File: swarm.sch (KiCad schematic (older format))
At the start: 28 parts, among them P1 USB_OTG, P2 CONN_01X05, P3 CONN_02X20, SW1 SW_PUSH, U1 LM3671MF-3.3, U2 STM32F103RETx, U3 APA102, Y1 Crystal

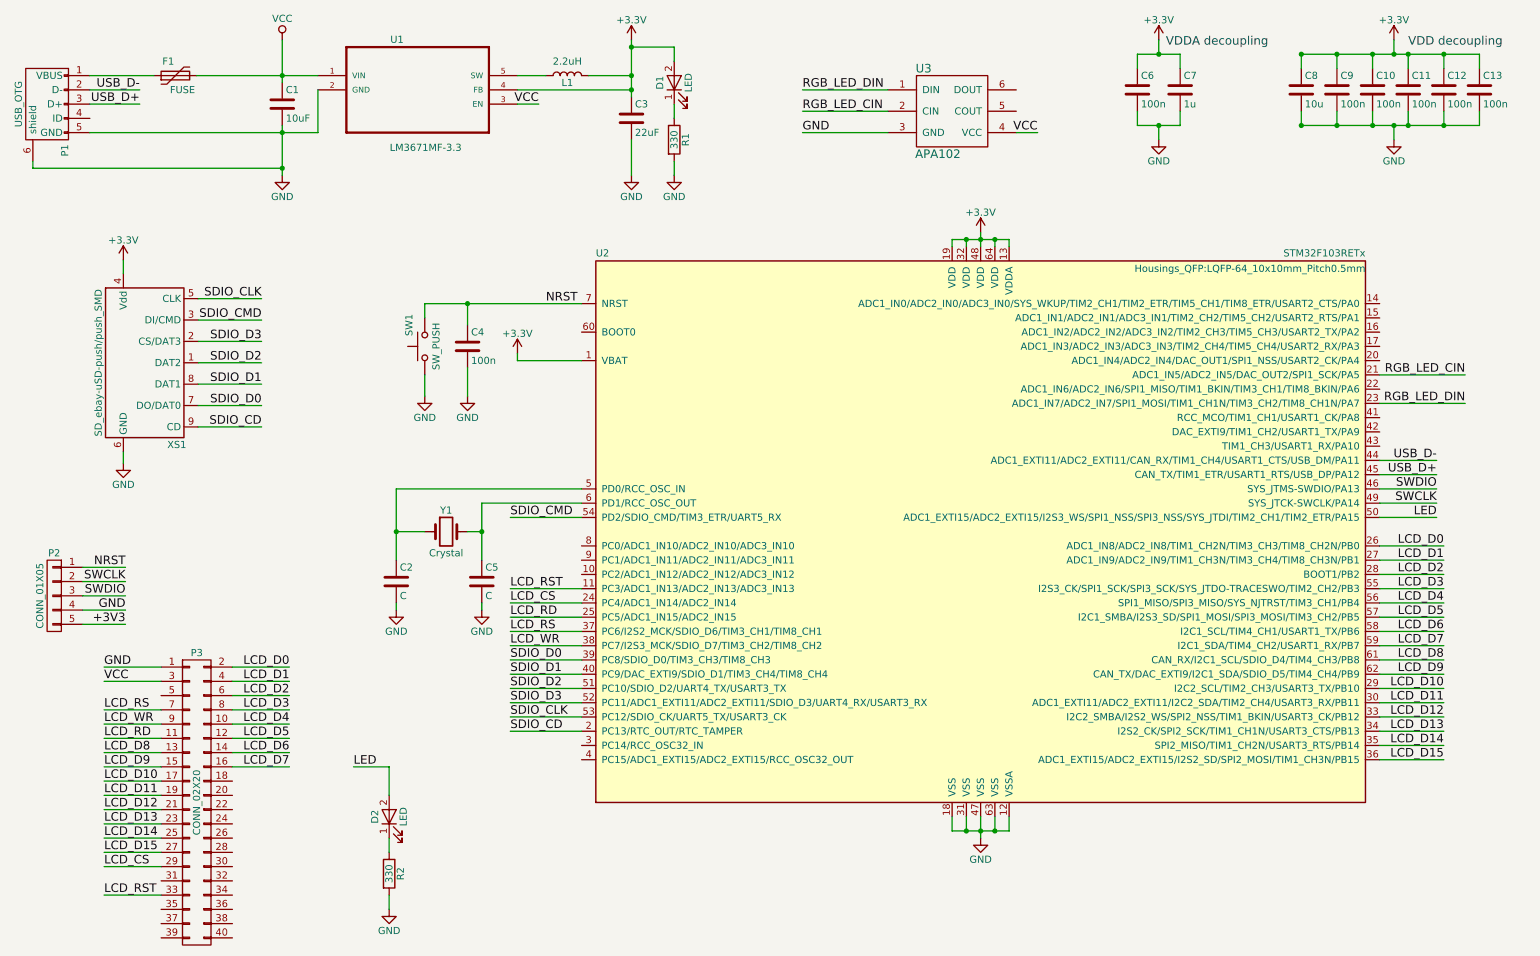
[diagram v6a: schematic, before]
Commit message: Connects 'BOOT0' pin (60) to ground Forgot to connect this pin in Rev 1.0, this pin need to be '0' to select Boot Mode "Main Flash memory" In layout, connected PIN 60 (BOOT0) to GND using 'via'
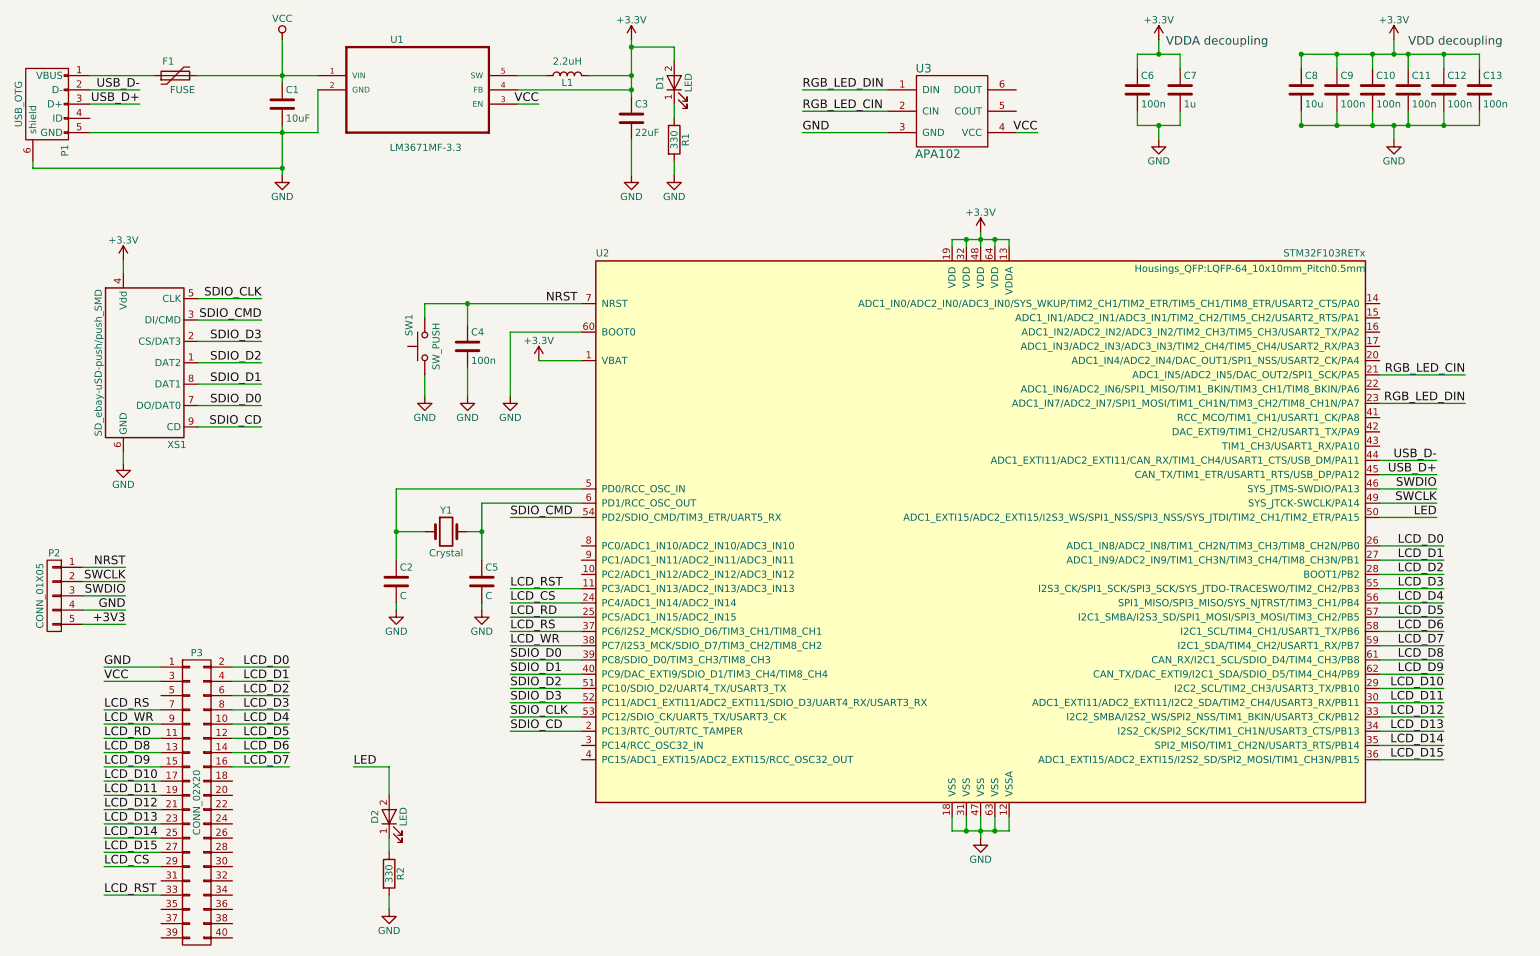
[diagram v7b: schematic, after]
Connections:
- net GND: now also U2.60 (BOOT0)
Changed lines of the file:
@@
 L +3.3V #PWR03
 U 1 1 581369FC
-P 4200 2950
-F 0 "#PWR03" H 4200 2800 50  0001 C CNN
-F 1 "+3.3V" H 4200 3090 50  0000 C CNN
-F 2 "" H 4200 2950 50  0000 C CNN
-F 3 "" H 4200 2950 50  0000 C CNN
-	1    4200 2950
+P 4350 3000
+F 0 "#PWR03" H 4350 2850 50  0001 C CNN
+F 1 "+3.3V" H 4350 3140 50  0000 C CNN
+F 2 "" H 4350 3000 50  0000 C CNN
+F 3 "" H 4350 3000 50  0000 C CNN
+	1    4350 3000
 	1    0    0    -1
 $EndComp
@@
 Connection ~ 7450 6300
 Wire Wire Line
-	7450 6200 7450 6350
+	7450 6200 7450 6300
+Wire Wire Line
+	7450 6300 7450 6350
 Connection ~ 7450 2150
 Wire Wire Line
@@
 Connection ~ 7550 2150
 Wire Wire Line
-	7450 2100 7450 2200
+	7450 2100 7450 2150
+Wire Wire Line
+	7450 2150 7450 2200
 Wire Wire Line
 	7350 2200 7350 2150
@@
 	7250 2150 7250 2200
 Wire Wire Line
-	7250 6300 7650 6300
+	7250 6300 7350 6300
+Wire Wire Line
+	7350 6300 7450 6300
+Wire Wire Line
+	7450 6300 7550 6300
+Wire Wire Line
+	7550 6300 7650 6300
 Wire Wire Line
 	7650 6300 7650 6200
@@
 Connection ~ 7550 6300
 Wire Wire Line
-	4650 3000 4200 3000
-Wire Wire Line
-	4200 3000 4200 2950
+	4650 3000 4350 3000
 Wire Wire Line
 	10700 850  10700 950
@@
 Connection ~ 10350 850
 Wire Wire Line
-	9700 1350 10950 1350
+	9700 1350 9950 1350
+Wire Wire Line
+	9950 1350 10200 1350
+Wire Wire Line
+	10200 1350 10350 1350
+Wire Wire Line
+	10350 1350 10450 1350
+Wire Wire Line
+	10450 1350 10700 1350
+Wire Wire Line
+	10700 1350 10950 1350
 Wire Wire Line
 	10700 1350 10700 1250
@@
 	3850 3050 3850 3250
 Wire Wire Line
-	3550 2600 4650 2600
+	3550 2600 3850 2600
+Wire Wire Line
+	3850 2600 4650 2600
 Wire Wire Line
 	3850 2600 3850 2750
@@
 	4650 3900 3350 3900
 Wire Wire Line
-	3350 3900 3350 4400
+	3350 3900 3350 4200
+Wire Wire Line
+	3350 4200 3350 4400
 Wire Wire Line
 	3350 4200 3550 4200
@@
 	3850 4200 3950 4200
 Wire Wire Line
-	3950 4000 3950 4400
+	3950 4000 3950 4200
+Wire Wire Line
+	3950 4200 3950 4400
 Wire Wire Line
 	3950 4750 3950 4700
@@
 Connection ~ 2550 1000
 Wire Wire Line
-	2550 1350 2550 1700
-Wire Wire Line
-	1200 1400 2800 1400
-Wire Wire Line
-	5000 750  5000 1150
+	2550 1350 2550 1400
+Wire Wire Line
+	2550 1400 2550 1650
+Wire Wire Line
+	2550 1650 2550 1700
+Wire Wire Line
+	1200 1400 2550 1400
+Wire Wire Line
+	2550 1400 2800 1400
+Wire Wire Line
+	5000 750  5000 800
+Wire Wire Line
+	5000 800  5000 1000
+Wire Wire Line
+	5000 1000 5000 1100
+Wire Wire Line
+	5000 1100 5000 1150
 Wire Wire Line
 	4200 1100 5000 1100
 Wire Wire Line
-	2550 750  2550 1050
+	2550 750  2550 1000
+Wire Wire Line
+	2550 1000 2550 1050
 Connection ~ 5000 1000
 Wire Wire Line
@@
 	4200 1200 4350 1200
 Wire Wire Line
-	1950 1000 2800 1000
+	1950 1000 2550 1000
+Wire Wire Line
+	2550 1000 2800 1000
 Connection ~ 5000 1100
 Wire Wire Line
@@
 	8550 1250 8550 1350
 Wire Wire Line
-	8550 1350 8850 1350
+	8550 1350 8700 1350
+Wire Wire Line
+	8700 1350 8850 1350
 Wire Wire Line
 	8850 1350 8850 1250
@@
 	8850 850  8850 950
 Wire Wire Line
-	8550 850  8850 850
+	8550 850  8700 850
+Wire Wire Line
+	8700 850  8850 850
 Wire Wire Line
 	8700 850  8700 750
@@
 	10250 3300 10850 3300
 Wire Wire Line
-	9700 850  10950 850
+	9700 850  9950 850
+Wire Wire Line
+	9950 850  10200 850
+Wire Wire Line
+	10200 850  10350 850
+Wire Wire Line
+	10350 850  10450 850
+Wire Wire Line
+	10450 850  10700 850
+Wire Wire Line
+	10700 850  10950 850
 Wire Wire Line
 	6800 1400 6200 1400
@@
 	10950 1350 10950 1250
 Wire Wire Line
-	7250 2150 7650 2150
+	7250 2150 7350 2150
+Wire Wire Line
+	7350 2150 7450 2150
+Wire Wire Line
+	7450 2150 7550 2150
+Wire Wire Line
+	7550 2150 7650 2150
 Wire Wire Line
 	7650 2150 7650 2200
@@
 Wire Wire Line
 	3550 2600 3550 2700
+Wire Wire Line
+	4650 2800 4150 2800
+Wire Wire Line
+	4150 2800 4150 3250
+$Comp
+L GND #PWR?
+U 1 1 587D4CBA
+P 4150 3250
+F 0 "#PWR?" H 4150 3000 50  0001 C CNN
+F 1 "GND" H 4150 3100 50  0000 C CNN
+F 2 "" H 4150 3250 50  0000 C CNN
+F 3 "" H 4150 3250 50  0000 C CNN
+	1    4150 3250
+	1    0    0    -1
+$EndComp
 $EndSCHEMATC

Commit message: Cosmetic change to schematic, regenerated net file
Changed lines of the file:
@@
 Connection ~ 7450 6300
 Wire Wire Line
-	7450 6200 7450 6300
-Wire Wire Line
-	7450 6300 7450 6350
+	7450 6200 7450 6350
 Connection ~ 7450 2150
 Wire Wire Line
@@
 Connection ~ 7550 2150
 Wire Wire Line
-	7450 2100 7450 2150
-Wire Wire Line
-	7450 2150 7450 2200
+	7450 2100 7450 2200
 Wire Wire Line
 	7350 2200 7350 2150
@@
 	7250 2150 7250 2200
 Wire Wire Line
-	7250 6300 7350 6300
-Wire Wire Line
-	7350 6300 7450 6300
-Wire Wire Line
-	7450 6300 7550 6300
-Wire Wire Line
-	7550 6300 7650 6300
+	7250 6300 7650 6300
 Wire Wire Line
 	7650 6300 7650 6200
@@
 Connection ~ 10350 850
 Wire Wire Line
-	9700 1350 9950 1350
-Wire Wire Line
-	9950 1350 10200 1350
-Wire Wire Line
-	10200 1350 10350 1350
-Wire Wire Line
-	10350 1350 10450 1350
-Wire Wire Line
-	10450 1350 10700 1350
-Wire Wire Line
-	10700 1350 10950 1350
+	9700 1350 10950 1350
 Wire Wire Line
 	10700 1350 10700 1250
@@
 	3850 3050 3850 3250
 Wire Wire Line
-	3550 2600 3850 2600
-Wire Wire Line
-	3850 2600 4650 2600
+	3550 2600 4650 2600
 Wire Wire Line
 	3850 2600 3850 2750
@@
 	4650 3900 3350 3900
 Wire Wire Line
-	3350 3900 3350 4200
-Wire Wire Line
-	3350 4200 3350 4400
+	3350 3900 3350 4400
 Wire Wire Line
 	3350 4200 3550 4200
@@
 	3850 4200 3950 4200
 Wire Wire Line
-	3950 4000 3950 4200
-Wire Wire Line
-	3950 4200 3950 4400
+	3950 4000 3950 4400
 Wire Wire Line
 	3950 4750 3950 4700
@@
 Connection ~ 2550 1000
 Wire Wire Line
-	2550 1350 2550 1400
-Wire Wire Line
-	2550 1400 2550 1650
-Wire Wire Line
-	2550 1650 2550 1700
-Wire Wire Line
-	1200 1400 2550 1400
-Wire Wire Line
-	2550 1400 2800 1400
-Wire Wire Line
-	5000 750  5000 800
-Wire Wire Line
-	5000 800  5000 1000
-Wire Wire Line
-	5000 1000 5000 1100
-Wire Wire Line
-	5000 1100 5000 1150
+	2550 1350 2550 1700
+Wire Wire Line
+	1200 1400 2800 1400
+Wire Wire Line
+	5000 750  5000 1150
 Wire Wire Line
 	4200 1100 5000 1100
 Wire Wire Line
-	2550 750  2550 1000
-Wire Wire Line
-	2550 1000 2550 1050
+	2550 750  2550 1050
 Connection ~ 5000 1000
 Wire Wire Line
@@
 	4200 1200 4350 1200
 Wire Wire Line
-	1950 1000 2550 1000
-Wire Wire Line
-	2550 1000 2800 1000
+	1950 1000 2800 1000
 Connection ~ 5000 1100
 Wire Wire Line
@@
 	8550 1250 8550 1350
 Wire Wire Line
-	8550 1350 8700 1350
-Wire Wire Line
-	8700 1350 8850 1350
+	8550 1350 8850 1350
 Wire Wire Line
 	8850 1350 8850 1250
@@
 	8850 850  8850 950
 Wire Wire Line
-	8550 850  8700 850
-Wire Wire Line
-	8700 850  8850 850
+	8550 850  8850 850
 Wire Wire Line
 	8700 850  8700 750
@@
 	10250 3300 10850 3300
 Wire Wire Line
-	9700 850  9950 850
-Wire Wire Line
-	9950 850  10200 850
-Wire Wire Line
-	10200 850  10350 850
-Wire Wire Line
-	10350 850  10450 850
-Wire Wire Line
-	10450 850  10700 850
-Wire Wire Line
-	10700 850  10950 850
+	9700 850  10950 850
 Wire Wire Line
 	6800 1400 6200 1400
@@
 	10950 1350 10950 1250
 Wire Wire Line
-	7250 2150 7350 2150
-Wire Wire Line
-	7350 2150 7450 2150
-Wire Wire Line
-	7450 2150 7550 2150
-Wire Wire Line
-	7550 2150 7650 2150
+	7250 2150 7650 2150
 Wire Wire Line
 	7650 2150 7650 2200
@@
 	4150 2800 4150 3250
 $Comp
-L GND #PWR?
+L GND #PWR020
 U 1 1 587D4CBA
 P 4150 3250
-F 0 "#PWR?" H 4150 3000 50  0001 C CNN
+F 0 "#PWR020" H 4150 3000 50  0001 C CNN
 F 1 "GND" H 4150 3100 50  0000 C CNN
 F 2 "" H 4150 3250 50  0000 C CNN
